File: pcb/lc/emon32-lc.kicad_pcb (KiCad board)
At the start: 4 copper layers, 55 x 40 mm, 72 parts, among them J1 AudioJack3_Ground_Switch, J2 AudioJack3_Ground_Switch, J3 Conn_02x05_Odd_Even, J4 RJ12, J5 Conn_Coaxial, J6 USB_C_Receptacle_USB2.0, J7 Conn_01x03_Male, J8 Conn_02x04_Odd_Even, J9 Conn_01x03_Male, SW1 SW_Push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

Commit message: * [PCB LC]
  - Change to MCP1501 reference
  - Some retouching of traces
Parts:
- removed U5: REF3012, Package_TO_SOT_SMD:SOT-23
- added U1: MCP1501-10xCH, Package_TO_SOT_SMD:SOT-23-6, F.Cu at (161.5, 126.5)
- moved J7 5.03 mm to (146.5, 129.5), turned to -90 degrees
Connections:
- J7 pad 1: /UART_DBG_TX -> /UART_DBG_RX
- J7 pad 2: /UART_DBG_RX -> /UART_DBG_TX
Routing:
- net Net-(C10-Pad1): track 3.45 -> 7.10 mm
- net /UART_DBG_RX: track 7.12 -> 3.67 mm
- net /UART_DBG_TX: track 10.4 -> 7.24 mm
- net +3V3: track 116.0 -> 117.9 mm
- net +5V: track 44.9 -> 45.7 mm
- net /V_REF: track 61.2 -> 60.7 mm

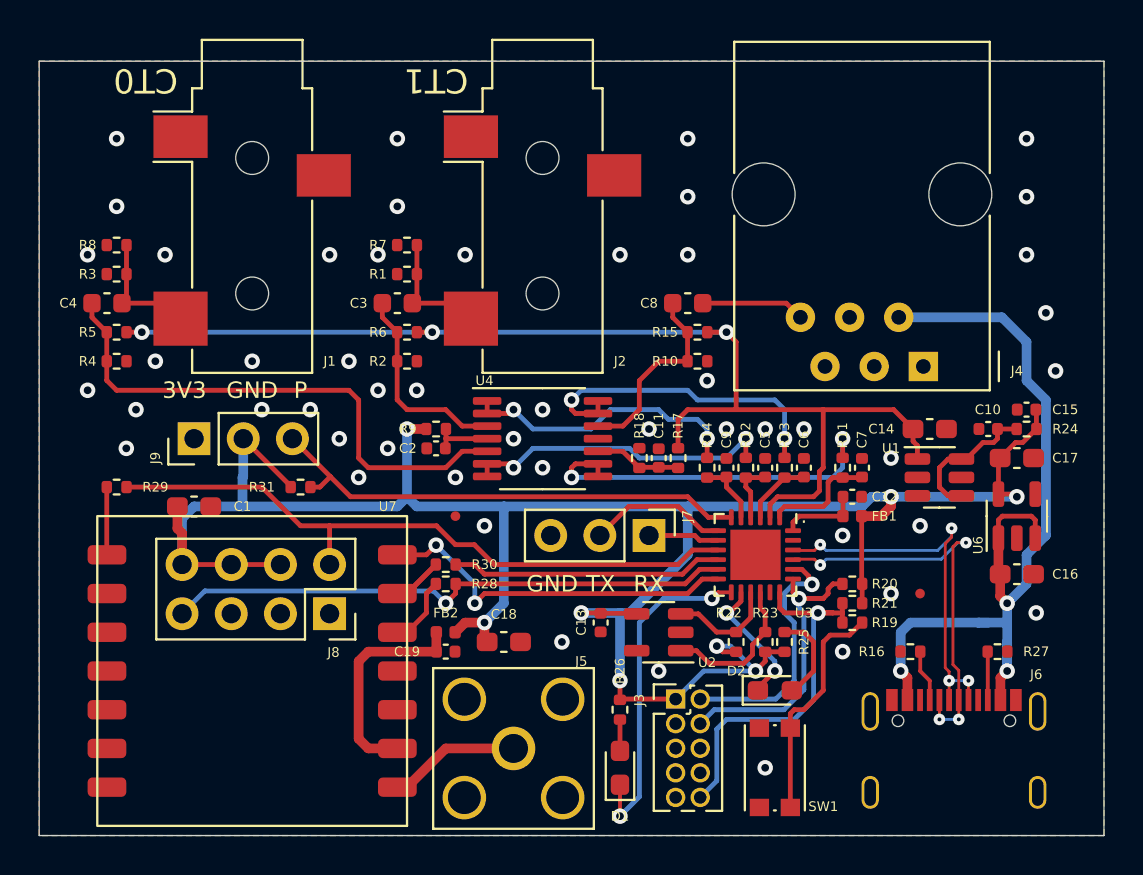
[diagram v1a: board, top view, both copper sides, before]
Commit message: * [PCB LC]
  - Revise USB routing/spacing
  - Remove CT current out burden resistors
  - Add AAF filter, revise ADC input filter values
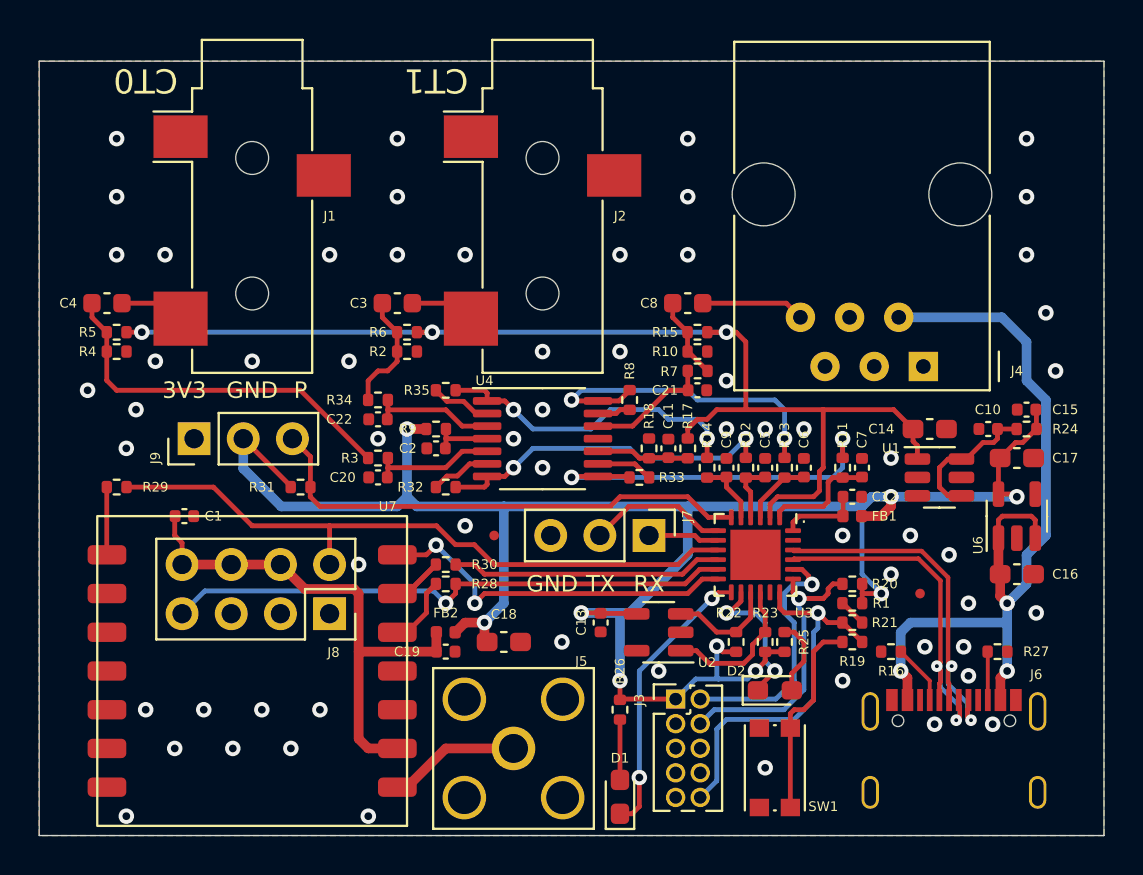
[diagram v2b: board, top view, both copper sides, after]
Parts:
- added C20: 10n, Capacitor_SMD:C_0402_1005Metric, F.Cu at (132.5, 126.5)
- added C21: 10n, Capacitor_SMD:C_0402_1005Metric, F.Cu at (149.0, 122.0)
- added C22: 10n, Capacitor_SMD:C_0402_1005Metric, F.Cu at (132.5, 123.5)
- added R32: 330R, Resistor_SMD:R_0402_1005Metric, F.Cu at (136.0, 127.0)
- added R33: 330R, Resistor_SMD:R_0402_1005Metric, F.Cu at (146.0, 126.5)
- added R34: 3K3, Resistor_SMD:R_0402_1005Metric, F.Cu at (132.5, 122.5)
- added R35: 330R, Resistor_SMD:R_0402_1005Metric, F.Cu at (136.0, 122.0)
- C1: value 2u2 -> 100n; footprint Capacitor_SMD:C_0603_1608Metric_Pad1.08x0.95mm_HandSolder -> Capacitor_SMD:C_0402_1005Metric
- C5, C6, C7, C9: value 10n -> 1n
- R1: value 22R -> 5K1
- R11, R12, R13, R14: value 3K3 -> 330R
- R21: value 10K -> 5K1
- R3, R7: value 22R -> 3K3
- R8: value 22R -> 330R
- moved R1 28.6 mm to (157.0, 133.0), turned to 180 degrees
- moved R8 27.7 mm to (145.5, 122.5), turned to 90 degrees
- moved R3 16.5 mm to (132.5, 125.5), turned to 180 degrees
- moved R7 16.4 mm to (149.0, 121.0), turned to 180 degrees
- moved FID2 2.24 mm to (138.5, 129.5)
- moved D1 1.50 mm to (145.0, 143.0)
- moved R16 1.00 mm to (159.0, 135.5)
- moved R19 1.00 mm to (157.0, 135.0), turned to 180 degrees
- moved R21 1.00 mm to (157.0, 134.0)
- moved C1 0.71 mm to (122.5, 128.5)
- moved C11 0.71 mm to (147.5, 125.0)
- moved R17 0.71 mm to (148.5, 125.0)
- moved R18 0.71 mm to (146.5, 125.0)
- moved R10 0.50 mm to (149.0, 120.0)
- moved R2 0.50 mm to (134.0, 120.0)
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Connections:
- C1 pad 1: +3V3 -> /3V3_TX
- C19 pad 1: Net-(C19-Pad1) -> /3V3_TX
- FB2 pad 1: Net-(C19-Pad1) -> /3V3_TX
- J8 pad 4: +3V3 -> /3V3_TX
- J8 pad 6: +3V3 -> /3V3_TX
- J8 pad 8: +3V3 -> /3V3_TX
- R1 pad 1: GND -> +3V3
- R1 pad 2: Net-(C3-Pad2) -> Net-(R1-Pad2)
- R21 pad 1: +3V3 -> Net-(R1-Pad2)
- R3 pad 1: GND -> Net-(C20-Pad2)
- R3 pad 2: Net-(C4-Pad2) -> Net-(C4-Pad1)
- R7 pad 1: GND -> Net-(C8-Pad1)
- R7 pad 2: Net-(C3-Pad2) -> Net-(C21-Pad2)
- R8 pad 1: GND -> Net-(R8-Pad1)
- R8 pad 2: Net-(C4-Pad2) -> Net-(R13-Pad1)
- U4 pad 12: Net-(C8-Pad1) -> Net-(C21-Pad2)
- U4 pad 13: Net-(R13-Pad1) -> Net-(R8-Pad1)
- U4 pad 2: Net-(R14-Pad2) -> Net-(R35-Pad2)
- U4 pad 3: Net-(C3-Pad1) -> Net-(C22-Pad2)
- U4 pad 5: Net-(C4-Pad1) -> Net-(C20-Pad2)
- U4 pad 6: Net-(R12-Pad2) -> Net-(R32-Pad2)
- U4 pad 9: Net-(R11-Pad2) -> Net-(R33-Pad2)
- U7 pad 2: Net-(C19-Pad1) -> /3V3_TX
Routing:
- net /3V3_TX: track 0.00 -> 27.1 mm
- net +3V3: track 117.9 -> 104.4 mm, vias 8 -> 9
- net Net-(C19-Pad1): track 11.4 -> 0.00 mm
- net Net-(C4-Pad1): track 27.9 -> 19.5 mm
- net Net-(C20-Pad2): track 0.00 -> 6.45 mm
- net Net-(C22-Pad2): track 0.00 -> 6.45 mm
- net Net-(C21-Pad2): track 0.00 -> 6.40 mm
- net Net-(C8-Pad1): track 10.2 -> 4.23 mm
- net Net-(C3-Pad1): track 10.5 -> 6.23 mm
- net Net-(R32-Pad2): track 0.00 -> 3.14 mm
- net Net-(R33-Pad2): track 0.00 -> 2.90 mm
- net /LED_STATUS: track 17.4 -> 14.6 mm
- net /USB_D-: track 21.3 -> 18.5 mm, vias 4 -> 2
- net Net-(C4-Pad2): track 4.99 -> 2.22 mm
- net Net-(C3-Pad2): track 4.99 -> 2.22 mm
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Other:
- board text added: "(c) Angus Logan 2023"
- board text added: "emon32-LC v0.1-dev"
- board text added: "github.com/awjlogan/emon32"
- board text removed: "Crow Road Ltd. 2023"
- board text removed: "emon32-LC v0.1"

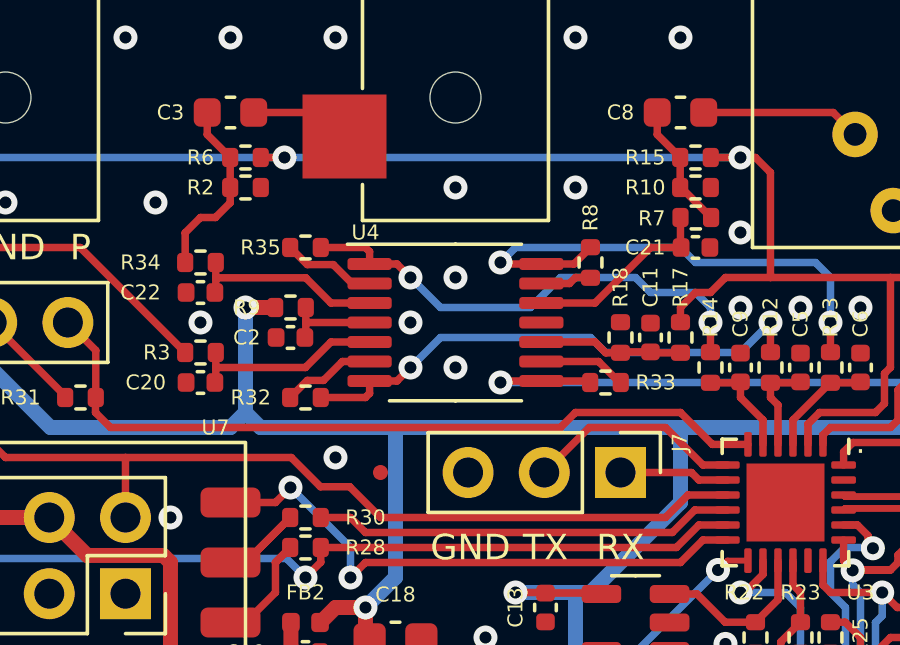
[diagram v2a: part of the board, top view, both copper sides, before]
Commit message: * [PCB LC]
  - Fix opamp bypass
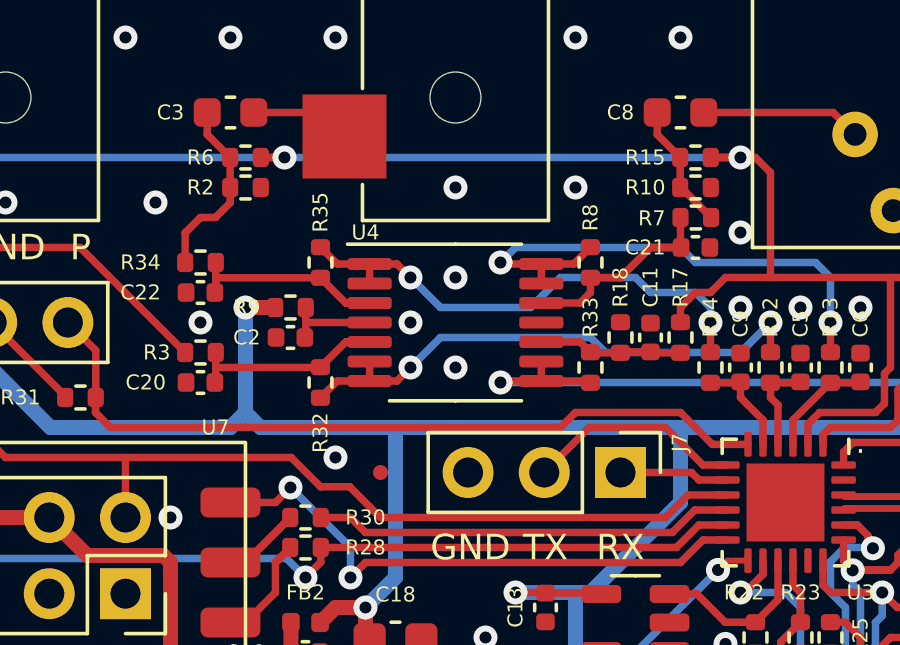
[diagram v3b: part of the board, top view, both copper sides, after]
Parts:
- R32, R33, R35, R8: value 330R -> 22R
- moved R32 0.71 mm to (136.5, 126.5), turned to 90 degrees
- moved R33 0.71 mm to (145.5, 126.0), turned to 90 degrees
- moved R35 0.71 mm to (136.5, 122.5), turned to -90 degrees
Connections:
- R13 pad 1: Net-(R13-Pad1) -> Net-(U4-Pad13)
- R32 pad 2: Net-(R32-Pad2) -> Net-(C20-Pad2)
- R33 pad 2: Net-(R33-Pad2) -> Net-(C11-Pad1)
- R35 pad 2: Net-(R35-Pad2) -> Net-(C22-Pad2)
- R8 pad 1: Net-(R8-Pad1) -> Net-(C21-Pad2)
- R8 pad 2: Net-(R13-Pad1) -> Net-(U4-Pad13)
- U4 pad 13: Net-(R8-Pad1) -> Net-(U4-Pad13)
- U4 pad 14: Net-(R13-Pad1) -> Net-(U4-Pad13)
- U4 pad 2: Net-(R35-Pad2) -> Net-(R14-Pad2)
- U4 pad 6: Net-(R32-Pad2) -> Net-(R12-Pad2)
- U4 pad 9: Net-(R33-Pad2) -> Net-(R11-Pad2)
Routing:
- net Net-(U4-Pad13): track 0.00 -> 18.0 mm, vias 0 -> 2
- net Net-(R13-Pad1): track 17.4 -> 0.00 mm, vias 2 -> 0
- net Net-(R32-Pad2): track 3.14 -> 0.00 mm
- net Net-(R33-Pad2): track 2.90 -> 0.00 mm
- net Net-(R35-Pad2): track 2.56 -> 0.00 mm
- net Net-(R8-Pad1): track 1.71 -> 0.00 mm
- net Net-(R11-Pad2): track 19.7 -> 20.4 mm

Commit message: * [PCB LC]
  - Final touch up for manufacture
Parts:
- moved R3 2.92 mm to (135.0, 127.0)
- moved C20 2.55 mm to (135.0, 126.0)
- moved C22 2.12 mm to (134.0, 122.0)
- moved R34 2.12 mm to (134.0, 121.0)
- moved C2 1.12 mm to (136.5, 124.5), turned to -90 degrees
- moved R9 0.50 mm to (135.0, 124.0)
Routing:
- net Net-(C4-Pad1): track 19.5 -> 22.6 mm
- net Net-(C20-Pad2): track 6.45 -> 3.97 mm
- net Net-(C3-Pad1): track 6.23 -> 3.82 mm
- net +3V3: track 104.4 -> 105.5 mm
- net Net-(C22-Pad2): track 6.45 -> 5.39 mm
- net GND: vias 61 -> 64

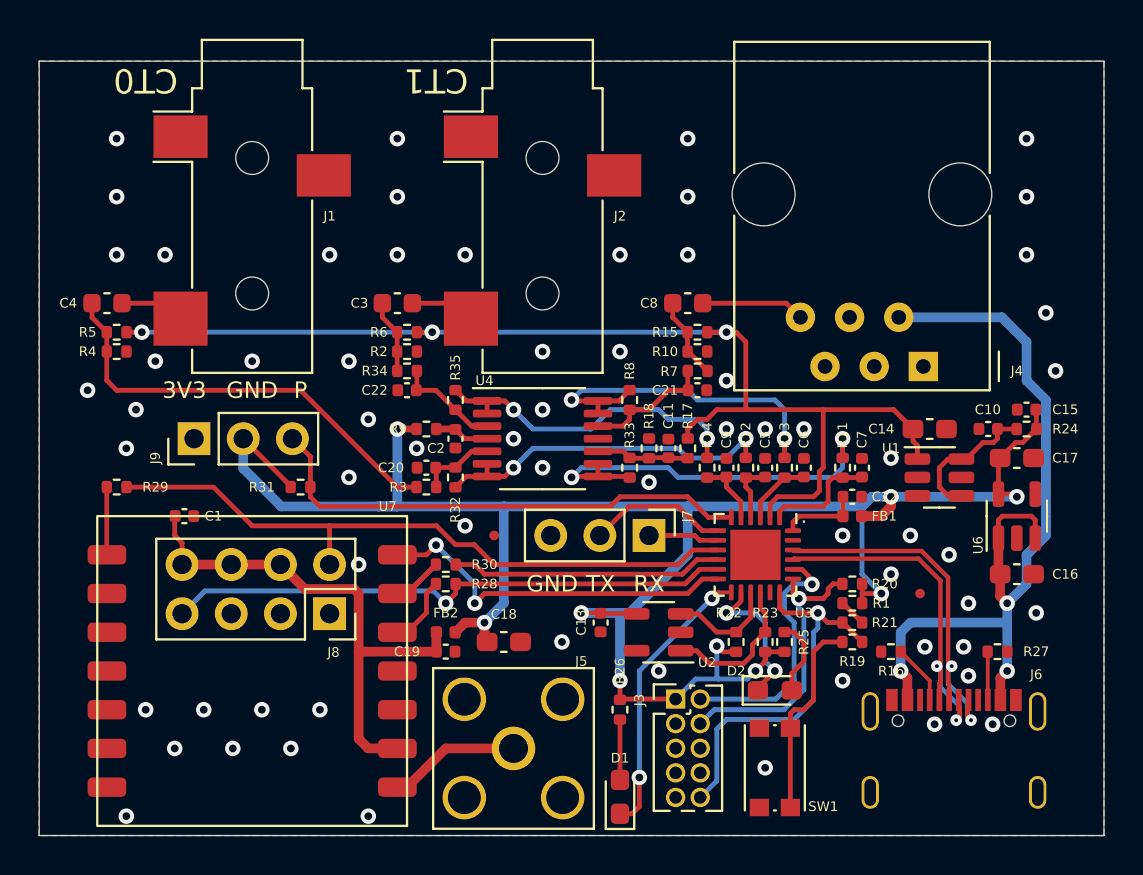
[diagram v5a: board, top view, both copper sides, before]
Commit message: * [PCB LC]
  - First iteration of changes from LC-0.1dev -> LC-0.1
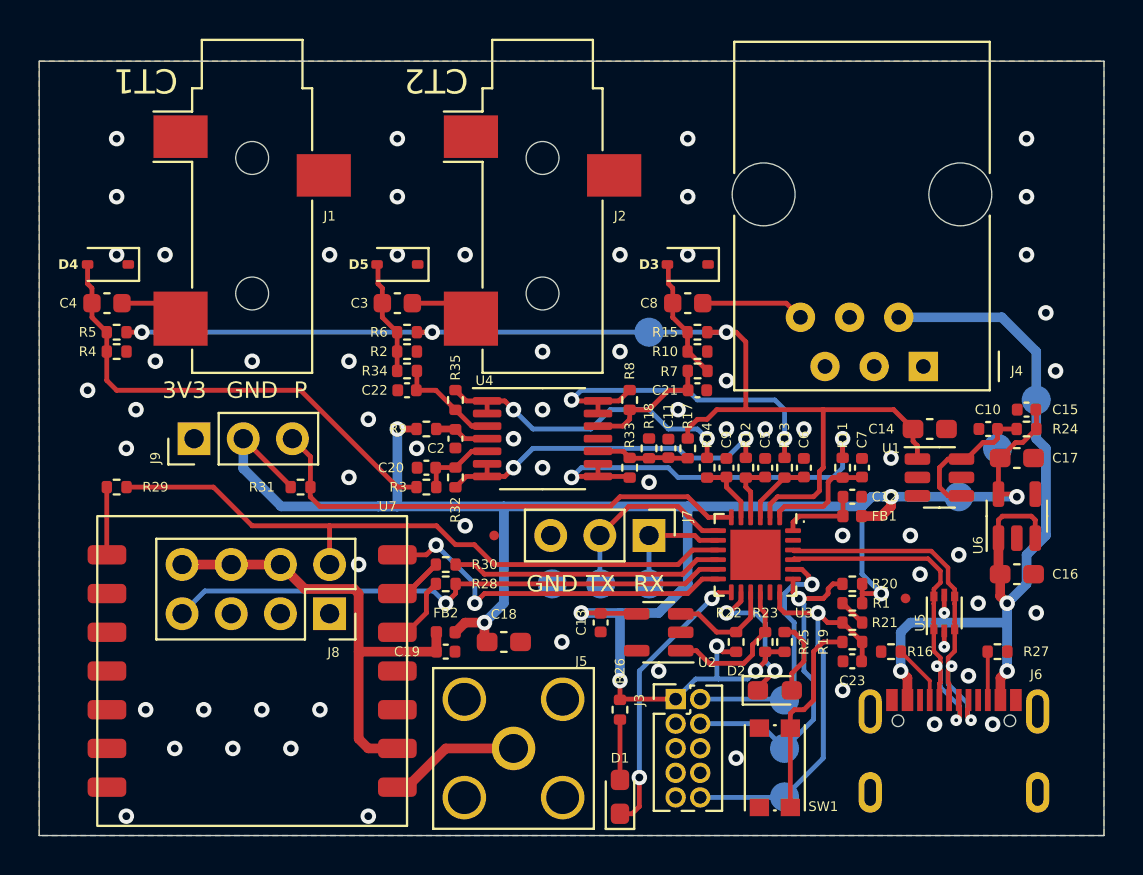
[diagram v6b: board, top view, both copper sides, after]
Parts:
- removed C1: 100n, Capacitor_SMD:C_0402_1005Metric
- added C23: 100n, Capacitor_SMD:C_0402_1005Metric, F.Cu at (157.0, 136.0)
- added D3: SD05_SOD323, Diode_SMD:D_SOD-323, F.Cu at (148.5, 115.5)
- added D4: SD05_SOD323, Diode_SMD:D_SOD-323, F.Cu at (118.5, 115.5)
- added D5: SD05_SOD323, Diode_SMD:D_SOD-323, F.Cu at (133.5, 115.5)
- added TP1: TestPoint, TestPoint:TestPoint_Pad_D1.5mm, B.Cu at (166.5, 122.5)
- added TP10: TestPoint, TestPoint:TestPoint_Pad_D1.5mm, B.Cu at (146.5, 132.0)
- added TP2: TestPoint, TestPoint:TestPoint_Pad_D1.5mm, B.Cu at (162.5, 127.5)
- added TP3: TestPoint, TestPoint:TestPoint_Pad_D1.5mm, B.Cu at (164.5, 125.0)
- added TP4: TestPoint, TestPoint:TestPoint_Pad_D1.5mm, B.Cu at (153.5, 140.5)
- added TP5: TestPoint, TestPoint:TestPoint_Pad_D1.5mm, B.Cu at (153.5, 138.0)
- added TP6: TestPoint, TestPoint:TestPoint_Pad_D1.5mm, B.Cu at (153.5, 143.0)
- added TP7: TestPoint, TestPoint:TestPoint_Pad_D1.5mm, B.Cu at (146.5, 119.0)
- added TP8: TestPoint, TestPoint:TestPoint_Pad_D1.5mm, B.Cu at (141.5, 132.0)
- added TP9: TestPoint, TestPoint:TestPoint_Pad_D1.5mm, B.Cu at (144.0, 132.0)
- added U5: USBLC6-2P6, Package_TO_SOT_SMD:SOT-666, F.Cu at (161.8, 133.5)
- C16, C17: value 2u2 -> 10u
- C5, C6, C7, C9: value 1n -> 10n
- R11, R12, R13, R14: value 330R -> 100R
- moved FID1 0.79 mm to (159.8, 132.8)
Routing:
- net /SWCLK: track 16.0 -> 18.7 mm
- net /3V3_TX: track 27.1 -> 24.5 mm
- net /UART_DBG_RX: track 3.67 -> 6.17 mm
- net /UART_DBG_TX: track 7.24 -> 9.70 mm
- net Net-(D4-A2): track 22.6 -> 24.7 mm
- net Net-(D5-A2): track 3.82 -> 5.86 mm
- net Net-(D3-A2): track 4.23 -> 6.27 mm
- net /~{RST}: track 19.9 -> 21.5 mm
- net +5V: track 43.7 -> 45.2 mm, vias 3 -> 4
- net +3V3: track 105.5 -> 106.4 mm
- net GND: track 0.00 -> 0.82 mm
- net /USB_D-: track 18.5 -> 19.1 mm
- net /USB_D+: track 19.2 -> 19.8 mm
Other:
- board text added: "(c) Tilt Ltd 2023"
- board text added: "5V"
- board text added: "CT2"
- board text added: "SWCLK"
- board text added: "SWDIO"
- board text added: "VREF"
- board text added: "emon32-LC v0.1"
- board text added: "~{RST}"
- board text removed: "(c) Angus Logan 2023"
- board text removed: "CT0"
- board text removed: "emon32-LC v0.1-dev"
